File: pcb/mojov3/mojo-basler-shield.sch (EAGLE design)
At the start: 9 parts

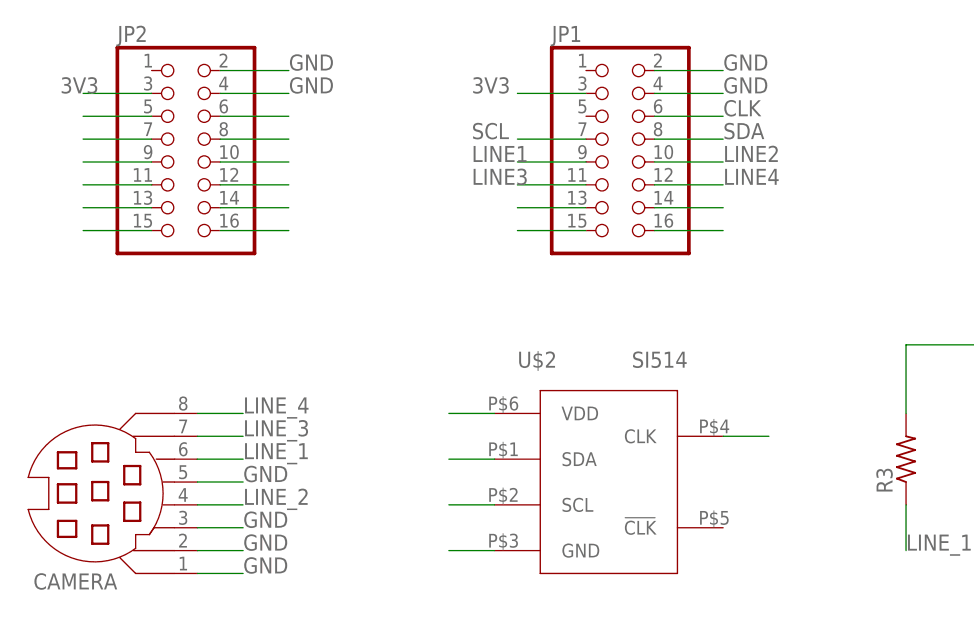
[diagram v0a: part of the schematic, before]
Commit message: finished basler camera adapter shield for mojo fpga board
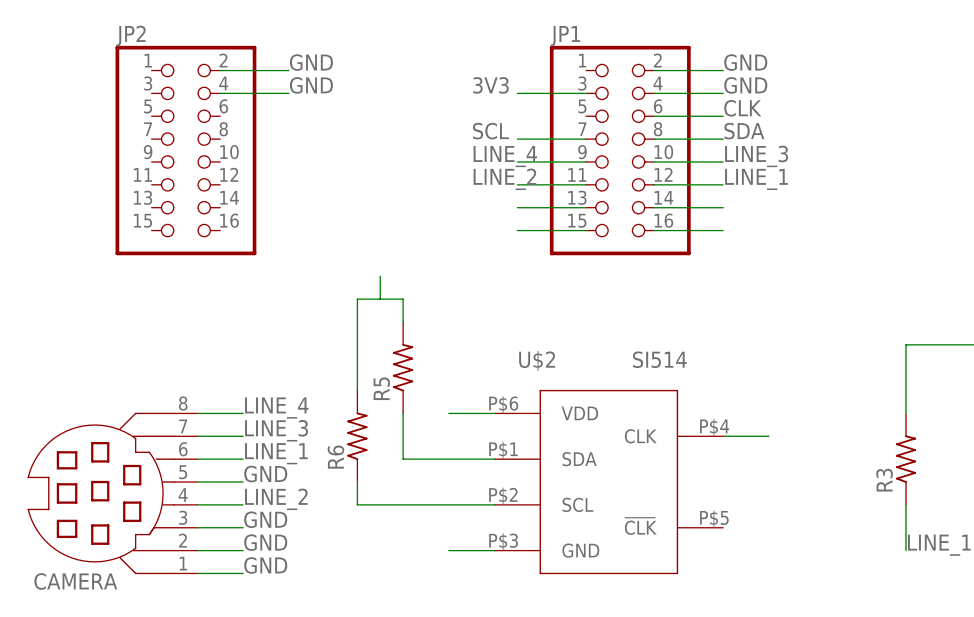
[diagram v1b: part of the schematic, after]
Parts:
- added R5, R6: (no value), rcl:R-US_R0603
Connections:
- removed net LINE1: JP1.9
- removed net LINE2: JP1.10
- removed net LINE3: JP1.11
- removed net LINE4: JP1.12
- removed net N$20: JP2.5
- removed net N$21: JP2.7
- removed net N$22: JP2.9
- removed net N$23: JP2.11
- removed net N$24: JP2.13
- removed net N$25: JP2.15
- removed net N$26: JP2.6
- removed net N$27: JP2.8
- removed net N$28: JP2.10
- removed net N$29: JP2.12
- removed net N$30: JP2.14
- removed net N$31: JP2.16
- net 3V3: now also R5.2, R6.2; no longer JP2.3
- net LINE_1: now also JP1.12
- net LINE_2: now also JP1.11
- net LINE_3: now also JP1.10
- net LINE_4: now also JP1.9
- net SCL: now also R6.1
- net SDA: now also R5.1
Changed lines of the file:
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@@
 <part name="R4" library="rcl" library_urn="urn:adsk.eagle:library:334" deviceset="R-US_" device="R0603" package3d_urn="urn:adsk.eagle:package:23555/2"/>
 <part name="U$2" library="lupa300-components" deviceset="SI514" device=""/>
+<part name="R5" library="rcl" library_urn="urn:adsk.eagle:library:334" deviceset="R-US_" device="R0603" package3d_urn="urn:adsk.eagle:package:23555/2"/>
+<part name="R6" library="rcl" library_urn="urn:adsk.eagle:library:334" deviceset="R-US_" device="R0603" package3d_urn="urn:adsk.eagle:package:23555/2"/>
 </parts>
 <sheets>
@@
 <instance part="R4" gate="G$1" x="152.4" y="25.4" rot="R90"/>
 <instance part="U$2" gate="G$1" x="73.66" y="22.86"/>
+<instance part="R5" gate="G$1" x="50.8" y="35.56" rot="R90"/>
+<instance part="R6" gate="G$1" x="45.72" y="27.94" rot="R90"/>
 </instances>
 <busses>
@@
 <label x="137.16" y="15.24" size="1.778" layer="95"/>
 </segment>
+<segment>
+<pinref part="JP1" gate="A" pin="10"/>
+<wire x1="78.74" y1="58.42" x2="86.36" y2="58.42" width="0.1524" layer="91"/>
+<label x="86.36" y="58.42" size="1.778" layer="95"/>
+</segment>
 </net>
 <net name="LINE_2" class="0">
@@
 <label x="121.92" y="15.24" size="1.778" layer="95"/>
 </segment>
+<segment>
+<pinref part="JP1" gate="A" pin="11"/>
+<wire x1="71.12" y1="55.88" x2="63.5" y2="55.88" width="0.1524" layer="91"/>
+<label x="58.42" y="55.88" size="1.778" layer="95"/>
+</segment>
 </net>
 <net name="LINE_1" class="0">
@@
 <label x="106.68" y="15.24" size="1.778" layer="95"/>
 </segment>
+<segment>
+<pinref part="JP1" gate="A" pin="12"/>
+<wire x1="78.74" y1="55.88" x2="86.36" y2="55.88" width="0.1524" layer="91"/>
+<label x="86.36" y="55.88" size="1.778" layer="95"/>
+</segment>
 </net>
 <net name="LINE_4" class="0">
@@
 <wire x1="152.4" y1="20.32" x2="152.4" y2="15.24" width="0.1524" layer="91"/>
 <label x="152.4" y="15.24" size="1.778" layer="95"/>
+</segment>
+<segment>
+<pinref part="JP1" gate="A" pin="9"/>
+<wire x1="71.12" y1="58.42" x2="63.5" y2="58.42" width="0.1524" layer="91"/>
+<label x="58.42" y="58.42" size="1.778" layer="95"/>
 </segment>
 </net>
@@
 </segment>
 <segment>
-<pinref part="JP2" gate="A" pin="3"/>
-<wire x1="22.86" y1="66.04" x2="15.24" y2="66.04" width="0.1524" layer="91"/>
-<label x="12.7" y="66.04" size="1.778" layer="95"/>
-</segment>
-<segment>
 <pinref part="U$2" gate="G$1" pin="VDD"/>
 <wire x1="60.96" y1="30.48" x2="55.88" y2="30.48" width="0.1524" layer="91"/>
+</segment>
+<segment>
+<pinref part="R6" gate="G$1" pin="2"/>
+<wire x1="45.72" y1="33.02" x2="45.72" y2="43.18" width="0.1524" layer="91"/>
+<wire x1="45.72" y1="43.18" x2="48.26" y2="43.18" width="0.1524" layer="91"/>
+<pinref part="R5" gate="G$1" pin="2"/>
+<wire x1="48.26" y1="43.18" x2="50.8" y2="43.18" width="0.1524" layer="91"/>
+<wire x1="50.8" y1="43.18" x2="50.8" y2="40.64" width="0.1524" layer="91"/>
+<wire x1="48.26" y1="43.18" x2="48.26" y2="45.72" width="0.1524" layer="91"/>
 </segment>
 </net>
@@
 <segment>
 <pinref part="U$2" gate="G$1" pin="SCL"/>
-<wire x1="60.96" y1="20.32" x2="55.88" y2="20.32" width="0.1524" layer="91"/>
-</segment>
-</net>
-<net name="LINE1" class="0">
-<segment>
-<pinref part="JP1" gate="A" pin="9"/>
-<wire x1="71.12" y1="58.42" x2="63.5" y2="58.42" width="0.1524" layer="91"/>
-<label x="58.42" y="58.42" size="1.778" layer="95"/>
-</segment>
-</net>
-<net name="LINE3" class="0">
-<segment>
-<pinref part="JP1" gate="A" pin="11"/>
-<wire x1="71.12" y1="55.88" x2="63.5" y2="55.88" width="0.1524" layer="91"/>
-<label x="58.42" y="55.88" size="1.778" layer="95"/>
+<wire x1="60.96" y1="20.32" x2="45.72" y2="20.32" width="0.1524" layer="91"/>
+<pinref part="R6" gate="G$1" pin="1"/>
+<wire x1="45.72" y1="20.32" x2="45.72" y2="22.86" width="0.1524" layer="91"/>
 </segment>
 </net>
@@
 <segment>
 <pinref part="U$2" gate="G$1" pin="SDA"/>
-<wire x1="60.96" y1="25.4" x2="55.88" y2="25.4" width="0.1524" layer="91"/>
-</segment>
-</net>
-<net name="LINE2" class="0">
-<segment>
-<pinref part="JP1" gate="A" pin="10"/>
-<wire x1="78.74" y1="58.42" x2="86.36" y2="58.42" width="0.1524" layer="91"/>
-<label x="86.36" y="58.42" size="1.778" layer="95"/>
-</segment>
-</net>
-<net name="LINE4" class="0">
-<segment>
-<pinref part="JP1" gate="A" pin="12"/>
-<wire x1="78.74" y1="55.88" x2="86.36" y2="55.88" width="0.1524" layer="91"/>
-<label x="86.36" y="55.88" size="1.778" layer="95"/>
+<wire x1="60.96" y1="25.4" x2="50.8" y2="25.4" width="0.1524" layer="91"/>
+<pinref part="R5" gate="G$1" pin="1"/>
+<wire x1="50.8" y1="25.4" x2="50.8" y2="30.48" width="0.1524" layer="91"/>
 </segment>
 </net>
@@
 </segment>
 </net>
-<net name="N$20" class="0">
-<segment>
-<pinref part="JP2" gate="A" pin="5"/>
-<wire x1="22.86" y1="63.5" x2="15.24" y2="63.5" width="0.1524" layer="91"/>
-</segment>
-</net>
-<net name="N$21" class="0">
-<segment>
-<pinref part="JP2" gate="A" pin="7"/>
-<wire x1="22.86" y1="60.96" x2="15.24" y2="60.96" width="0.1524" layer="91"/>
-</segment>
-</net>
-<net name="N$22" class="0">
-<segment>
-<pinref part="JP2" gate="A" pin="9"/>
-<wire x1="22.86" y1="58.42" x2="15.24" y2="58.42" width="0.1524" layer="91"/>
-</segment>
-</net>
-<net name="N$23" class="0">
-<segment>
-<pinref part="JP2" gate="A" pin="11"/>
-<wire x1="22.86" y1="55.88" x2="15.24" y2="55.88" width="0.1524" layer="91"/>
-</segment>
-</net>
-<net name="N$24" class="0">
-<segment>
-<pinref part="JP2" gate="A" pin="13"/>
-<wire x1="22.86" y1="53.34" x2="15.24" y2="53.34" width="0.1524" layer="91"/>
-</segment>
-</net>
-<net name="N$25" class="0">
-<segment>
-<pinref part="JP2" gate="A" pin="15"/>
-<wire x1="22.86" y1="50.8" x2="15.24" y2="50.8" width="0.1524" layer="91"/>
-</segment>
-</net>
-<net name="N$26" class="0">
-<segment>
-<pinref part="JP2" gate="A" pin="6"/>
-<wire x1="30.48" y1="63.5" x2="38.1" y2="63.5" width="0.1524" layer="91"/>
-</segment>
-</net>
-<net name="N$27" class="0">
-<segment>
-<pinref part="JP2" gate="A" pin="8"/>
-<wire x1="30.48" y1="60.96" x2="38.1" y2="60.96" width="0.1524" layer="91"/>
-</segment>
-</net>
-<net name="N$28" class="0">
-<segment>
-<pinref part="JP2" gate="A" pin="10"/>
-<wire x1="30.48" y1="58.42" x2="38.1" y2="58.42" width="0.1524" layer="91"/>
-</segment>
-</net>
-<net name="N$29" class="0">
-<segment>
-<pinref part="JP2" gate="A" pin="12"/>
-<wire x1="30.48" y1="55.88" x2="38.1" y2="55.88" width="0.1524" layer="91"/>
-</segment>
-</net>
-<net name="N$30" class="0">
-<segment>
-<pinref part="JP2" gate="A" pin="14"/>
-<wire x1="30.48" y1="53.34" x2="38.1" y2="53.34" width="0.1524" layer="91"/>
-</segment>
-</net>
-<net name="N$31" class="0">
-<segment>
-<pinref part="JP2" gate="A" pin="16"/>
-<wire x1="30.48" y1="50.8" x2="38.1" y2="50.8" width="0.1524" layer="91"/>
-</segment>
-</net>

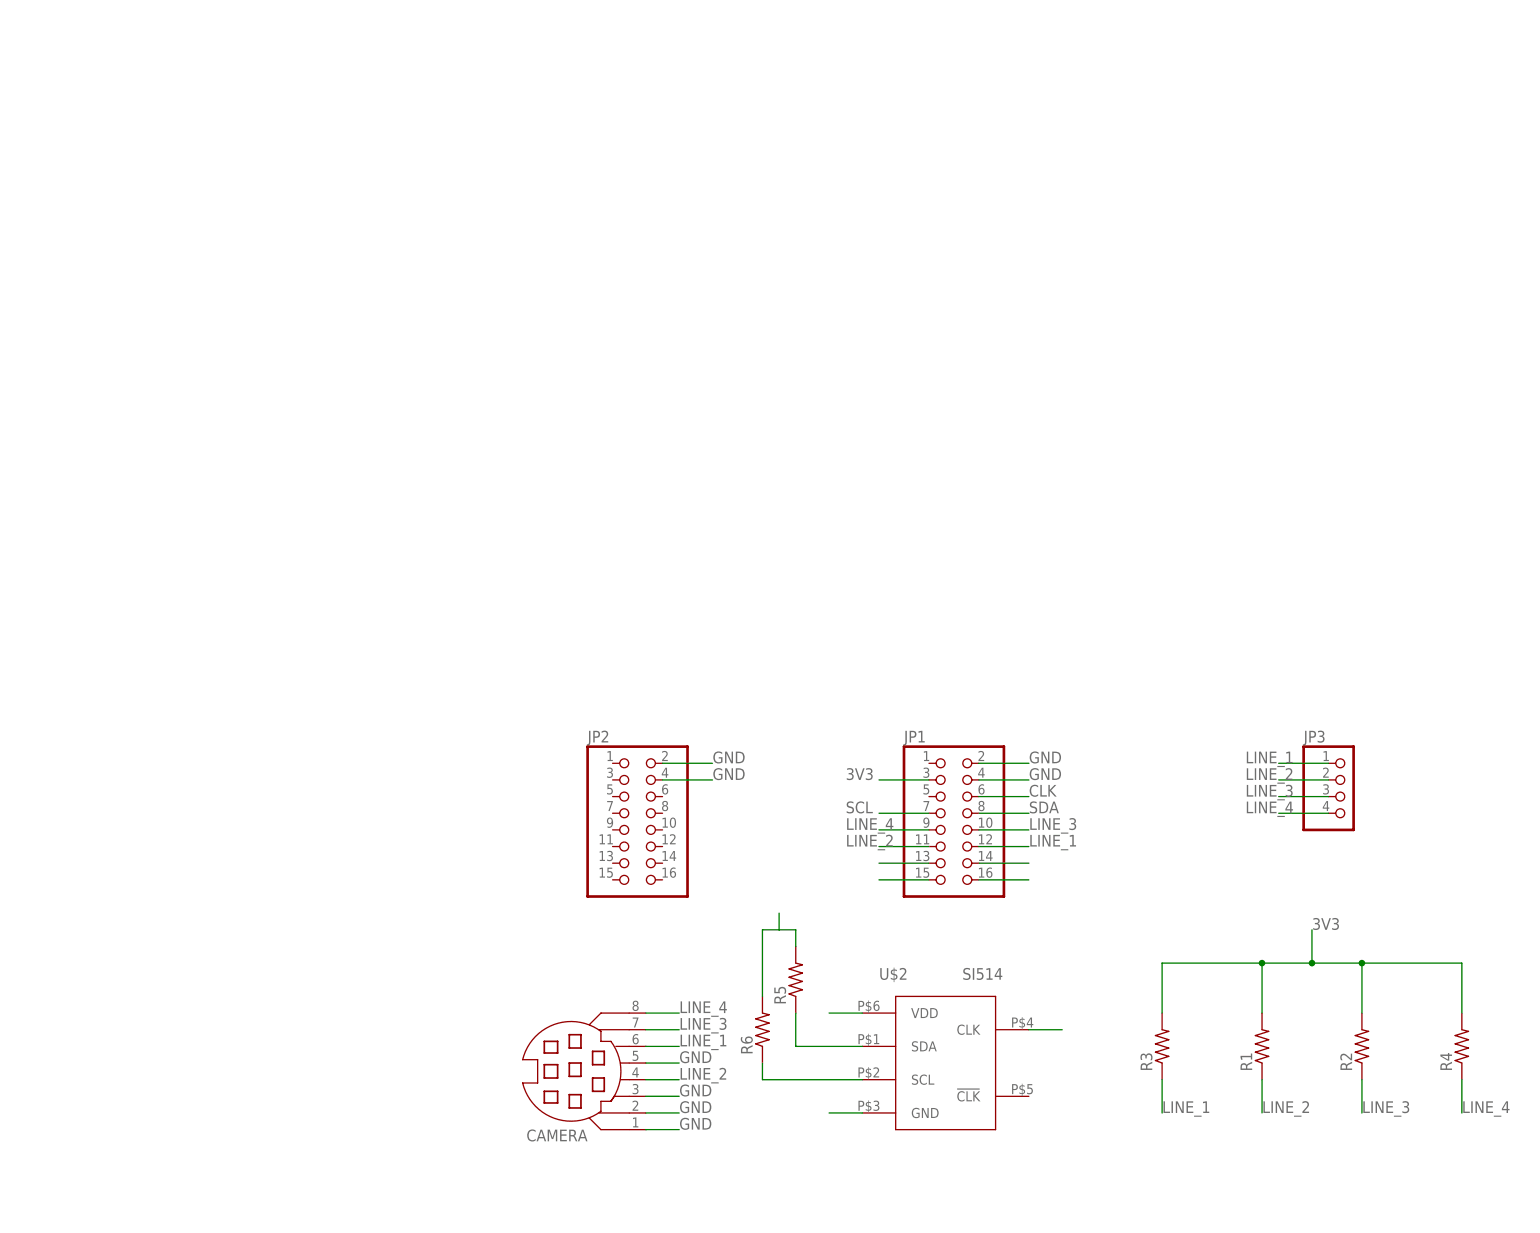
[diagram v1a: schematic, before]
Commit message: switched to full coverage shield with new pinouts
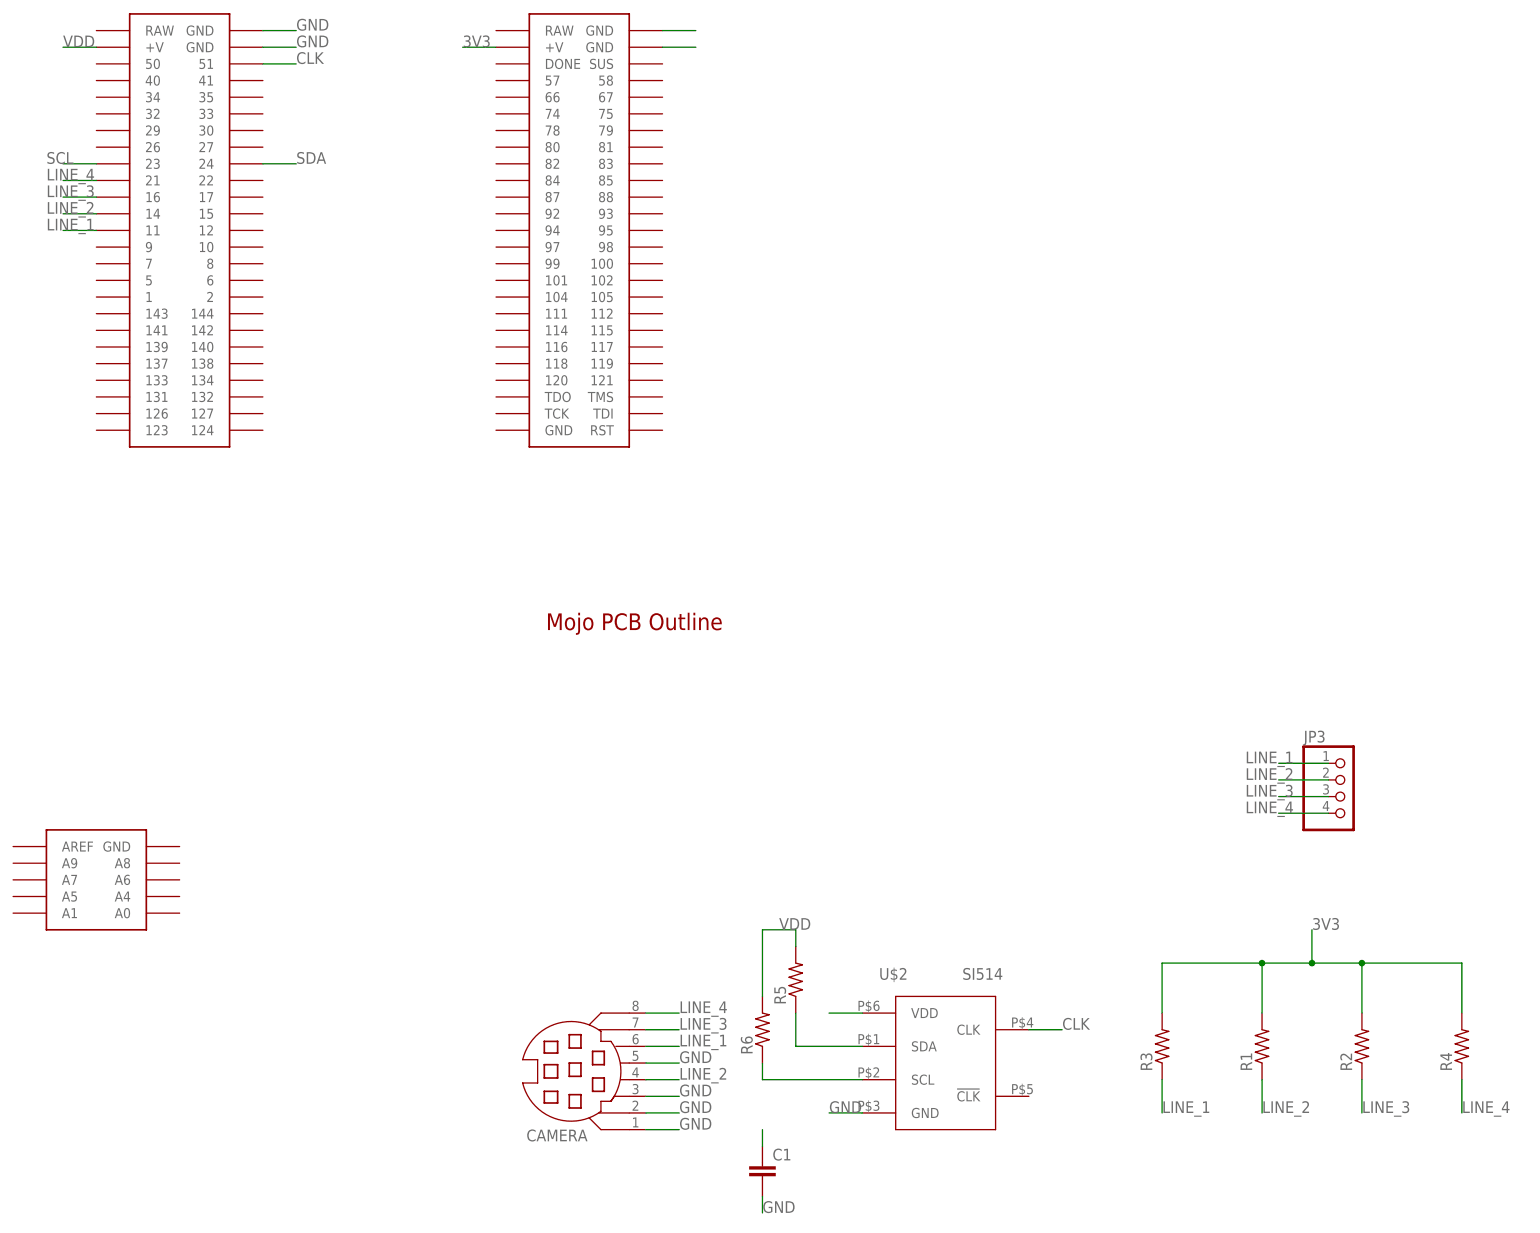
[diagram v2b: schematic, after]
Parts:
- removed JP1, JP2: (no value), pinhead:PINHD-2X8
- added C1: (no value), rcl:C-EUC0603
- added U$1: MOJO_OUTLINE, EmbeddedMicro-Mojo:MOJO_OUTLINE
- added U$3: MOJOV3, EmbeddedMicro-Mojo:MOJOV3
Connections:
- removed net N$13: JP1.13
- removed net N$14: JP1.15
- removed net N$18: JP1.14
- removed net N$19: JP1.16
- new net VDD: C1.1, R5.2, R6.2, U$2.VDD, U$3G$2.+V
- net 3V3: now also U$3G$3.+V; no longer JP1.3, R5.2, R6.2, U$2.VDD
- net CLK: now also U$3G$2.51; no longer JP1.6
- net GND: now also C1.2, U$3G$2.GND@1, U$3G$2.GND@2, U$3G$3.GND@1, U$3G$3.GND@2; no longer JP1.2, JP1.4, JP2.2, JP2.4
- net LINE_1: now also U$3G$2.11; no longer JP1.12
- net LINE_2: now also U$3G$2.14; no longer JP1.11
- net LINE_3: now also U$3G$2.16; no longer JP1.10
- net LINE_4: now also U$3G$2.21; no longer JP1.9
- net SCL: now also U$3G$2.23; no longer JP1.7
- net SDA: now also U$3G$2.24; no longer JP1.8
